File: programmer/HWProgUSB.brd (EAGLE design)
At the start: 80 x 52.4 mm, 98 parts, among them X2 P_AVR_P

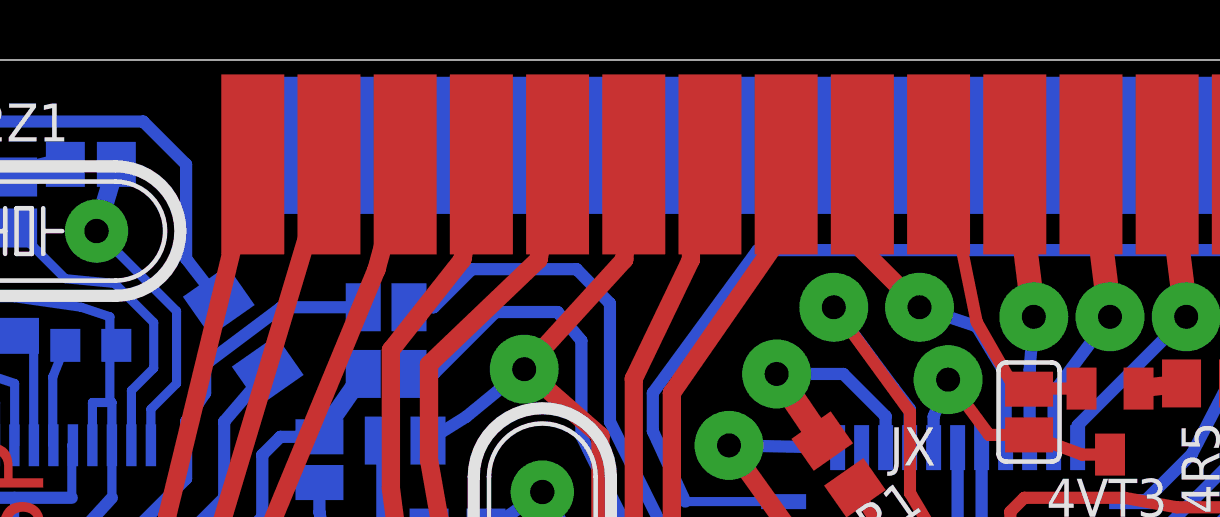
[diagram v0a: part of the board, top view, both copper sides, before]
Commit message: add 3v3 led ..
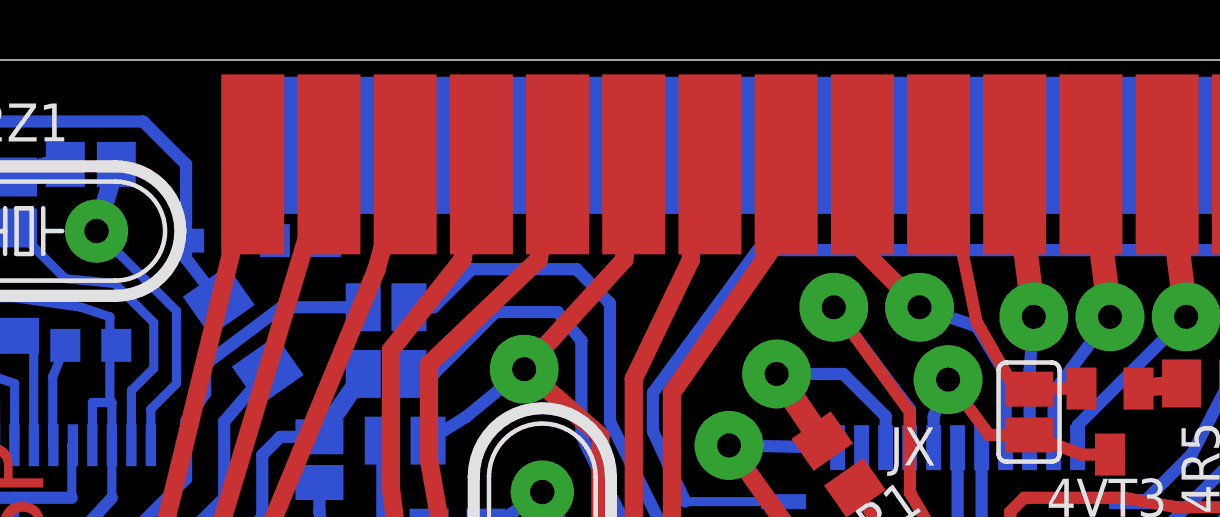
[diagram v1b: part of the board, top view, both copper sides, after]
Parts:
- added 2R11: (no value), resistor:R0603
- added LED3V3: (no value), led:CHIPLED_0603
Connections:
- new net N$22: 2R11.1, LED3V3.A
- net 3VUSB: now also LED3V3.C
- net GND: now also 2R11.2
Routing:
- net GND: track 369.2 -> 396.0 mm
- net N$22: track 0.00 -> 1.26 mm
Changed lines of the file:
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@@
 <setting verticaltext="up"/>
 </settings>
-<grid distance="25" unitdist="mil" unit="mm" style="lines" multiple="1" display="yes" altdistance="0.025" altunitdist="inch" altunit="inch"/>
+<grid distance="12.5" unitdist="mil" unit="mil" style="lines" multiple="1" display="yes" altdistance="0.025" altunitdist="inch" altunit="inch"/>
 <layers>
-<layer number="1" name="Top" color="4" fill="1" visible="yes" active="yes"/>
+<layer number="1" name="Top" color="4" fill="1" visible="no" active="yes"/>
 <layer number="2" name="Route2" color="1" fill="3" visible="no" active="no"/>
 <layer number="3" name="Route3" color="4" fill="3" visible="no" active="no"/>
@@
 </element>
 <element name="2C1" library="resistor" package="C0805" value="20" x="12.065" y="48.895" smashed="yes" rot="MR180">
-<attribute name="NAME" x="10.2235" y="51.3715" size="1.27" layer="26" rot="MR180"/>
+<attribute name="NAME" x="7.0485" y="50.419" size="1.27" layer="26" rot="MR180"/>
 <attribute name="VALUE" x="11.176" y="51.181" size="1.27" layer="28" rot="MR180"/>
 </element>
 <element name="2C2" library="resistor" package="C0805" value="20" x="9.525" y="47.625" smashed="yes" rot="MR270">
-<attribute name="NAME" x="6.4135" y="51.054" size="1.27" layer="26" rot="MR180"/>
+<attribute name="NAME" x="6.604" y="51.689" size="1.27" layer="26" rot="MR270"/>
 <attribute name="VALUE" x="11.811" y="48.514" size="1.27" layer="28" rot="MR270"/>
 </element>
@@
 </element>
 <element name="JR" library="jumper" package="SJ" value="" x="19.685" y="39.0525" smashed="yes" rot="MR270">
-<attribute name="NAME" x="16.4465" y="39.497" size="1.27" layer="26" ratio="10" rot="MR180"/>
+<attribute name="NAME" x="16.129" y="39.8145" size="1.27" layer="26" ratio="10" rot="MR180"/>
 <attribute name="VALUE" x="19.685" y="38.6524" size="0.02" layer="28" rot="MR270"/>
 </element>
@@
 </element>
 <element name="RJ5" library="rcl" package="R1206" value="0" x="17.145" y="43.18" smashed="yes" rot="MR55">
-<attribute name="NAME" x="19.866265625" y="45.72561875" size="1.27" layer="26" rot="MR0"/>
+<attribute name="NAME" x="19.231265625" y="42.23311875" size="1.27" layer="26" rot="MR55"/>
 <attribute name="VALUE" x="18.650296875" y="44.492790625" size="1.27" layer="28" rot="MR0"/>
 </element>
@@
 <element name="HW" library="HWProgUSB" package="PINHEAD_1X02" value="High Voltage Enable" x="62.07125" y="22.70125" rot="R270"/>
 <element name="3C5" library="rcl" package="C025-025X050" value="100n" x="50.8" y="7.62" rot="R270"/>
+<element name="2R11" library="resistor" package="R0603" value="" x="19.05" y="46.355" smashed="yes" rot="MR180">
+<attribute name="NAME" x="20.701" y="47.0535" size="1.27" layer="26" rot="MR180"/>
+<attribute name="VALUE" x="18.161" y="48.387" size="1.27" layer="28" rot="MR180"/>
+</element>
+<element name="LED3V3" library="led" package="CHIPLED_0603" value="" x="16.1925" y="46.355" smashed="yes" rot="MR270">
+<attribute name="NAME" x="16.1925" y="50.8" size="1.27" layer="26" rot="MR0"/>
+<attribute name="VALUE" x="17.4625" y="44.45" size="1.27" layer="28" rot="MR0"/>
+</element>
 </elements>
 <signals>
@@
 <wire x1="44.7675" y1="11.938" x2="45.847" y2="11.938" width="1.016" layer="16"/>
 <wire x1="45.847" y1="11.938" x2="50.8" y2="8.89" width="1.016" layer="16"/>
+<contactref element="2R11" pad="2"/>
+<wire x1="19.9" y1="46.355" x2="19.9" y2="49.53" width="0.4064" layer="16"/>
+<wire x1="19.9" y1="49.53" x2="43.4975" y2="49.53" width="0.4064" layer="16"/>
 <wire x1="40.9575" y1="29.21" x2="45.085" y2="33.655" width="0" layer="19" extent="16-16"/>
 </signal>
@@
 <contactref element="RJ5" pad="2"/>
 <wire x1="16.329375" y1="44.34483125" x2="15.24" y2="45.75170625" width="0.4064" layer="16"/>
-<wire x1="15.24" y1="45.75170625" x2="15.24" y2="48.895" width="0.4064" layer="16"/>
+<wire x1="15.24" y1="45.75170625" x2="15.24" y2="46.355" width="0.4064" layer="16"/>
+<wire x1="15.24" y1="46.355" x2="15.24" y2="48.895" width="0.4064" layer="16"/>
 <wire x1="15.24" y1="48.895" x2="13.81125" y2="50.32375" width="0.4064" layer="16"/>
 <wire x1="13.81125" y1="50.32375" x2="4.70625" y2="50.32375" width="0.4064" layer="16"/>
@@
 <wire x1="3.175" y1="49.8475" x2="4.1275" y2="49.90375" width="0.4064" layer="16"/>
 <wire x1="4.70625" y1="50.32375" x2="4.1275" y2="49.90375" width="0.4064" layer="16"/>
+<contactref element="LED3V3" pad="C"/>
+<wire x1="15.4425" y1="46.355" x2="15.24" y2="46.355" width="0.4064" layer="16"/>
 </signal>
 <signal name="N$58">
@@
 <wire x1="46.9875" y1="41.4225" x2="48.42125" y2="41.5925" width="0.6096" layer="1"/>
 </signal>
+<signal name="N$22">
+<contactref element="2R11" pad="1"/>
+<contactref element="LED3V3" pad="A"/>
+<wire x1="16.9425" y1="46.355" x2="18.2" y2="46.355" width="0.4064" layer="16"/>
+</signal>
 </signals>
